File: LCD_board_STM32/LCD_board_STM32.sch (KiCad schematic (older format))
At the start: 74 parts, among them CON1 PIN-2x4, CON2 PIN-2x4, CON3 PIN-2x4, CON4 SWD-6pin, CON5 PIN-1x2, Q1 PDTC114ET, Q2 CSTCE, SW1 MicroswitchSmt6x4_V, SW2 MicroswitchSmt6x4_V, SW3 MicroswitchSmt6x4_V, U1 STM32_LQFP48, U2 TFT_1_8_ST7735, U3 NCS199A1, U4 NCS199A1, U5 AMS1117-3.3, U6 LP2980AIM5-3.0

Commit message: Working on circuit.
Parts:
- removed C10: C, 0805_M, symbol C
- added C19, C20, C21, C22: 100n, 0603_N, symbol C
- added C23, C24, C25: C, 0805_N, symbol C
- added C26: C, 0603_N, symbol C
- added Q3, Q4, Q5, Q6: FDC6331L, SOT23-6_N, symbol FDC6331L
- added R38, R39, R40, R41: R, 0603_R_N, symbol R
- C18: footprint 0805_M -> 0805_N
- C9: value C -> 100n; footprint 0805_M -> 0603_N
- gave numbers to parts that had none: 1
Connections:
- net GND: now also U1.35 (PF6/VSS), C19.2, C20.2, C21.2, C22.2, C23.2, C24.2, C25.2, C26.2, Q3.1 (R2), Q4.1 (R2), Q5.1 (R2), Q6.1 (R2), R38.1
- net PIN10: now also Q5.2 (OUT), Q5.3 (OUT)
- net PIN11: now also Q6.2 (OUT), Q6.3 (OUT)
- net PIN8: now also Q3.2 (OUT), Q3.3 (OUT)
- net PIN9: now also Q4.2 (OUT), Q4.3 (OUT)
- net VCC: now also U1.36 (PF7/VDD/VDDIO2/VDD_USB), C19.1, C20.1, C21.1, C22.1, C23.1, C24.1, C25.1, R39.2
- net VPP: now also Q3.4 (Vin), Q4.4 (Vin), Q5.4 (Vin), Q6.4 (Vin)
- net uC10: now also Q5.5 (IN)
- net uC11: now also Q6.5 (IN)
- net uC8: now also Q3.5 (IN)
- net uC9: now also Q4.5 (IN)
- net at U1.17 (PA7/VDD): now also R40.2
- net at U1.25 (PB12/VREFSD+): now also C26.1, R39.1, R41.1
- net at U1.44 (PF11/PH3/BOOT0): now also R38.2
- no-connect marks 1 -> 5
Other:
- moved on the sheet: Q2

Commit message: Working on circuit.
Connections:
- net SWO is gone; now on net SWO/SCK: CON4.6 (SWO), U1.39 (PB3)
- net PIN4: now also U3.5 (IN-); no longer U3.4 (IN+)
- net PIN5: now also U3.4 (IN+); no longer U3.5 (IN-)
- net PIN6: now also U4.5 (IN-); no longer U4.4 (IN+)
- net PIN7: now also U4.4 (IN+); no longer U4.5 (IN-)
- net SW1: now also U1.10 (PA0)
- net SW2: now also U1.38 (PA15)
- net SW3: now also U1.20 (PB2/NPOR)
- net uC0: now also U1.46 (PB9); no longer U1.10 (PA0)
- net uC10: now also U1.45 (PB8)
- net uC11: now also U1.21 (PB10/PE8)
- net uC7: now also R40.1; no longer U1.18 (PB0)
- net uC8: now also U1.18 (PB0)
- net uC9: now also U1.19 (PB1)
- net TFT_CS: now reaches U2.12 (CS)
- net TFT_CS: now also U1.2 (PC13)
- net MOSI: now reaches U2.8 (SDA)
- net MOSI: now also U1.41 (PB5)
- net SWO/SCK: now reaches U2.9 (SCK)
- net uC12: now reaches U1.22 (PB11/PE9)
- net MISO: now reaches U1.40 (PB4)
- net SD_CS: now reaches U1.3 (PC14/OSC32_IN)
- net TFT_LED: now reaches U1.4 (PC15/OSC32_OUT)
- net at D1.2 (C): now also R41.2
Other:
- moved on the sheet: D1, U2

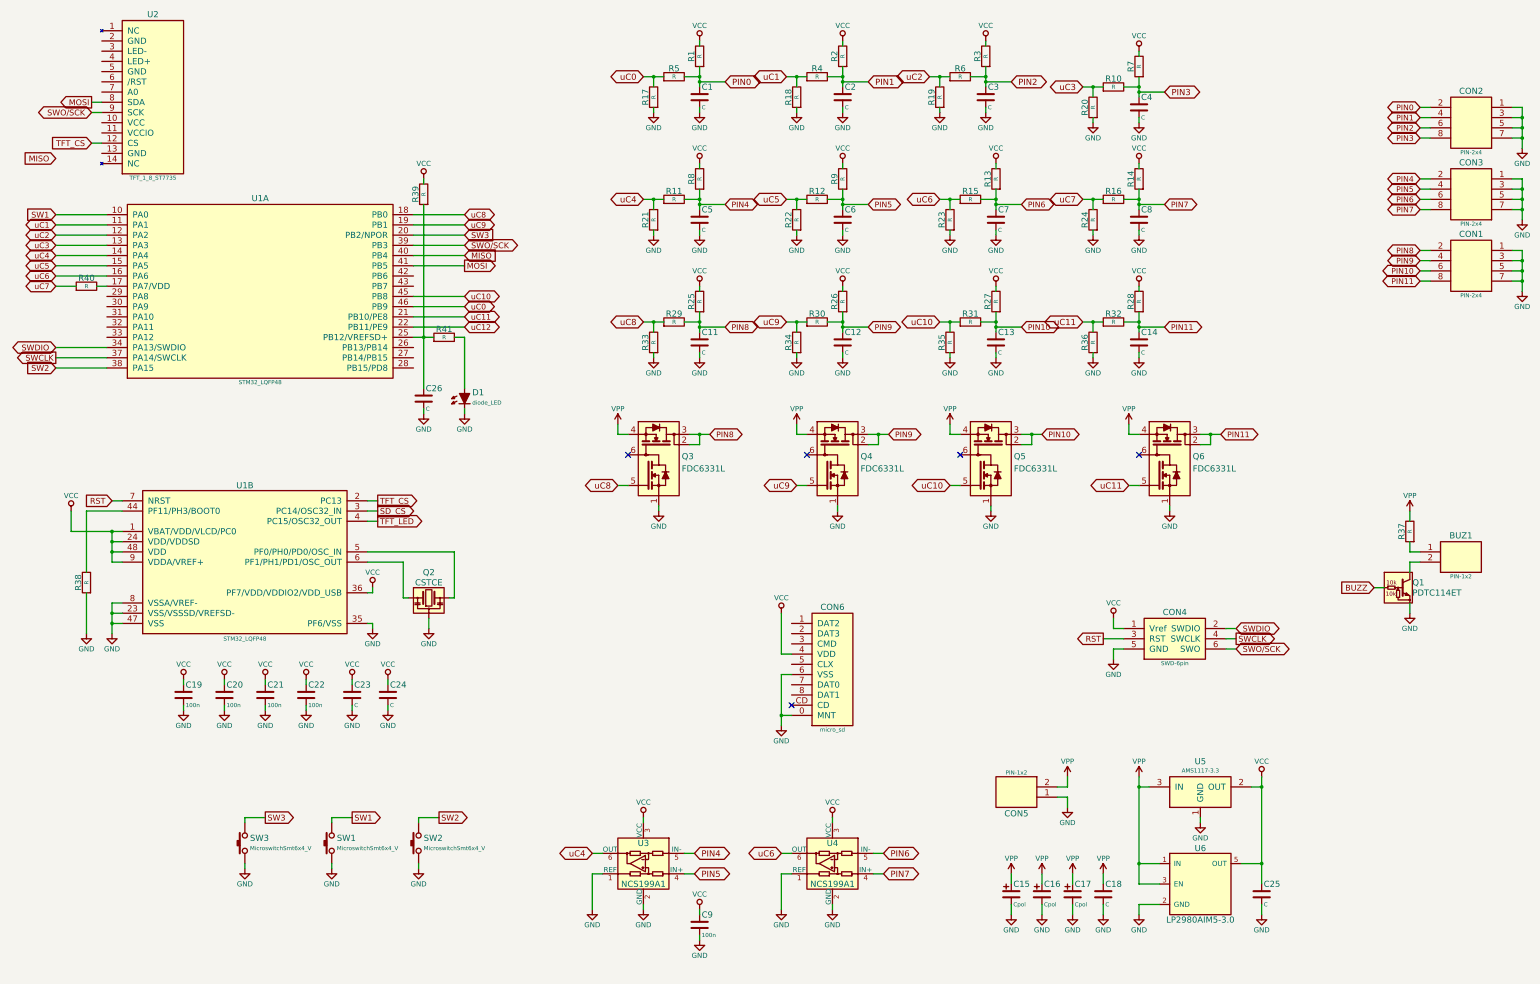
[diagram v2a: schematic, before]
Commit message: Rename nets
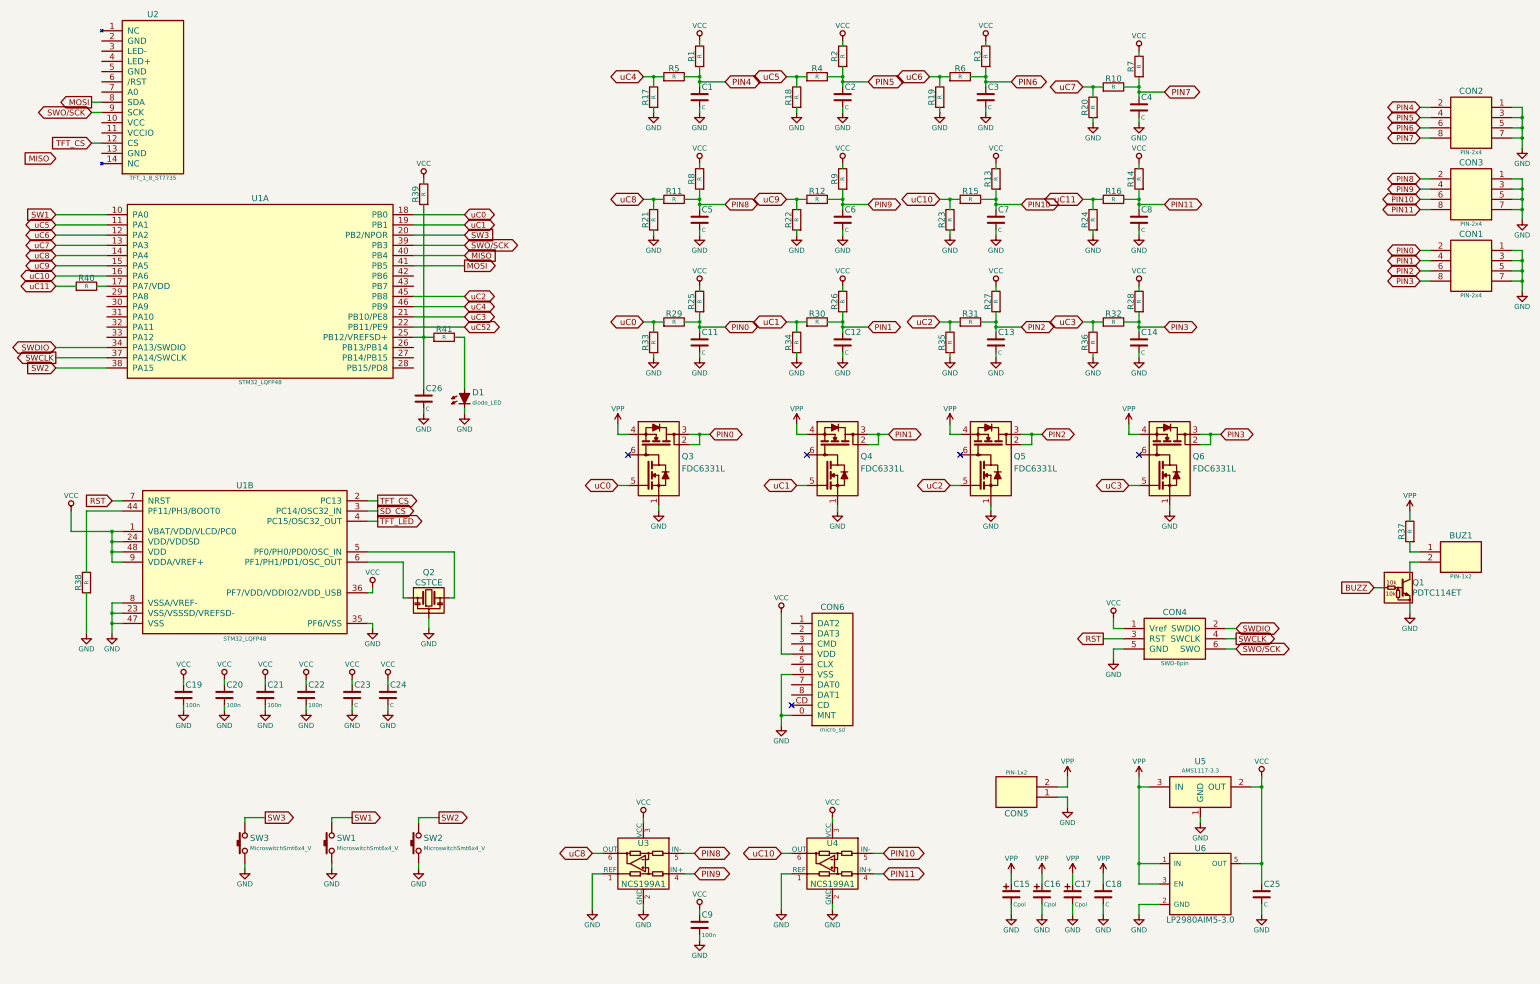
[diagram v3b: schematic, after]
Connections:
- net PIN0: now also C11.1, CON1.2, Q3.2 (OUT), Q3.3 (OUT), R25.1, R29.2; no longer C1.1, CON2.2, R1.1, R5.2
- net PIN1: now also C12.1, CON1.4, Q4.2 (OUT), Q4.3 (OUT), R26.1, R30.2; no longer C2.1, CON2.4, R2.1, R4.2
- net PIN10: now also C7.1, CON3.6, R13.1, R15.2, U4.5 (IN-); no longer C13.1, CON1.6, Q5.2 (OUT), Q5.3 (OUT), R27.1, R31.2
- net PIN11: now also C8.1, CON3.8, R14.1, R16.2, U4.4 (IN+); no longer C14.1, CON1.8, Q6.2 (OUT), Q6.3 (OUT), R28.1, R32.2
- net PIN2: now also C13.1, CON1.6, Q5.2 (OUT), Q5.3 (OUT), R27.1, R31.2; no longer C3.1, CON2.6, R3.1, R6.2
- net PIN3: now also C14.1, CON1.8, Q6.2 (OUT), Q6.3 (OUT), R28.1, R32.2; no longer C4.1, CON2.8, R10.2, R7.1
- net PIN4: now also C1.1, CON2.2, R1.1, R5.2; no longer C5.1, CON3.2, R11.2, R8.1, U3.5 (IN-)
- net PIN5: now also C2.1, CON2.4, R2.1, R4.2; no longer C6.1, CON3.4, R12.2, R9.1, U3.4 (IN+)
- net PIN6: now also C3.1, CON2.6, R3.1, R6.2; no longer C7.1, CON3.6, R13.1, R15.2, U4.5 (IN-)
- net PIN7: now also C4.1, CON2.8, R10.2, R7.1; no longer C8.1, CON3.8, R14.1, R16.2, U4.4 (IN+)
- net PIN8: now also C5.1, CON3.2, R11.2, R8.1, U3.5 (IN-); no longer C11.1, CON1.2, Q3.2 (OUT), Q3.3 (OUT), R25.1, R29.2
- net PIN9: now also C6.1, CON3.4, R12.2, R9.1, U3.4 (IN+); no longer C12.1, CON1.4, Q4.2 (OUT), Q4.3 (OUT), R26.1, R30.2
- net uC0: now also Q3.5 (IN), R29.1, R33.2, U1.18 (PB0); no longer R17.2, R5.1, U1.46 (PB9)
- net uC1: now also Q4.5 (IN), R30.1, R34.2, U1.19 (PB1); no longer R18.2, R4.1, U1.11 (PA1)
- net uC10: now also R15.1, R23.2, U1.16 (PA6), U4.6 (OUT); no longer Q5.5 (IN), R31.1, R35.2, U1.45 (PB8)
- net uC11: now also R16.1, R24.2, R40.1; no longer Q6.5 (IN), R32.1, R36.2, U1.21 (PB10/PE8)
- net uC2: now also Q5.5 (IN), R31.1, R35.2, U1.45 (PB8); no longer R19.2, R6.1, U1.12 (PA2)
- net uC3: now also Q6.5 (IN), R32.1, R36.2, U1.21 (PB10/PE8); no longer R10.1, R20.2, U1.13 (PA3)
- net uC4: now also R17.2, R5.1, U1.46 (PB9); no longer R11.1, R21.2, U1.14 (PA4), U3.6 (OUT)
- net uC5: now also R18.2, R4.1, U1.11 (PA1); no longer R12.1, R22.2, U1.15 (PA5)
- net uC6: now also R19.2, R6.1, U1.12 (PA2); no longer R15.1, R23.2, U1.16 (PA6), U4.6 (OUT)
- net uC7: now also R10.1, R20.2, U1.13 (PA3); no longer R16.1, R24.2, R40.1
- net uC8: now also R11.1, R21.2, U1.14 (PA4), U3.6 (OUT); no longer Q3.5 (IN), R29.1, R33.2, U1.18 (PB0)
- net uC9: now also R12.1, R22.2, U1.15 (PA5); no longer Q4.5 (IN), R30.1, R34.2, U1.19 (PB1)
- net uC12 renamed uC52
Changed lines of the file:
@@
 $EndComp
 Text GLabel 6900 1200 0    60   BiDi ~ 0
-uC0
+uC4
 Text GLabel 7700 1250 2    60   BiDi ~ 0
-PIN0
+PIN4
 Text GLabel 14500 2300 0    55   BiDi ~ 0
+PIN9
+Text GLabel 14500 2200 0    55   BiDi ~ 0
+PIN8
+Text GLabel 14500 2500 0    55   BiDi ~ 0
+PIN11
+Text GLabel 14500 2400 0    55   BiDi ~ 0
+PIN10
+Text GLabel 14500 1600 0    55   BiDi ~ 0
 PIN5
-Text GLabel 14500 2200 0    55   BiDi ~ 0
+Text GLabel 14500 1500 0    55   BiDi ~ 0
 PIN4
-Text GLabel 14500 2500 0    55   BiDi ~ 0
+Text GLabel 14500 1800 0    55   BiDi ~ 0
 PIN7
-Text GLabel 14500 2400 0    55   BiDi ~ 0
+Text GLabel 14500 1700 0    55   BiDi ~ 0
 PIN6
-Text GLabel 14500 1600 0    55   BiDi ~ 0
-PIN1
-Text GLabel 14500 1500 0    55   BiDi ~ 0
-PIN0
-Text GLabel 14500 1800 0    55   BiDi ~ 0
-PIN3
-Text GLabel 14500 1700 0    55   BiDi ~ 0
-PIN2
 $Comp
 L GND #PWR03
@@
 $EndComp
 Text GLabel 5150 3450 2    55   BiDi ~ 0
+uC4
+Text GLabel 1150 2650 0    55   BiDi ~ 0
+uC5
+Text GLabel 1150 2750 0    55   BiDi ~ 0
+uC6
+Text GLabel 1150 2850 0    55   BiDi ~ 0
+uC7
+Text GLabel 1150 2950 0    55   BiDi ~ 0
+uC8
+Text GLabel 1150 3050 0    55   BiDi ~ 0
+uC9
+Text GLabel 5150 2550 2    55   BiDi ~ 0
 uC0
-Text GLabel 1150 2650 0    55   BiDi ~ 0
-uC1
-Text GLabel 1150 2750 0    55   BiDi ~ 0
-uC2
-Text GLabel 1150 2850 0    55   BiDi ~ 0
-uC3
-Text GLabel 1150 2950 0    55   BiDi ~ 0
-uC4
-Text GLabel 1150 3050 0    55   BiDi ~ 0
-uC5
-Text GLabel 5150 2550 2    55   BiDi ~ 0
-uC8
 Text GLabel 1150 3150 0    55   BiDi ~ 0
-uC6
+uC10
 $Comp
 L R R4
@@
 $EndComp
 Text GLabel 8300 1200 0    60   BiDi ~ 0
-uC1
+uC5
 Text GLabel 9100 1250 2    60   BiDi ~ 0
-PIN1
+PIN5
 $Comp
 L R R6
@@
 $EndComp
 Text GLabel 9700 1200 0    60   BiDi ~ 0
-uC2
+uC6
 Text GLabel 10500 1250 2    60   BiDi ~ 0
-PIN2
+PIN6
 $Comp
 L R R10
@@
 $EndComp
 Text GLabel 11200 1300 0    60   BiDi ~ 0
-uC3
+uC7
 Text GLabel 12000 1350 2    60   BiDi ~ 0
-PIN3
+PIN7
 $Comp
 L R R11
@@
 $EndComp
 Text GLabel 6900 2400 0    60   BiDi ~ 0
-uC4
+uC8
 Text GLabel 7400 8800 2    60   BiDi ~ 0
-PIN4
+PIN8
 $Comp
 L R R12
@@
 $EndComp
 Text GLabel 8300 2400 0    60   BiDi ~ 0
-uC5
+uC9
 Text GLabel 7400 9000 2    60   BiDi ~ 0
-PIN5
+PIN9
 $Comp
 L R R15
@@
 $EndComp
 Text GLabel 9800 2400 0    60   BiDi ~ 0
-uC6
+uC10
 Text GLabel 9250 8800 2    60   BiDi ~ 0
-PIN6
+PIN10
 $Comp
 L R R16
@@
 $EndComp
 Text GLabel 11200 2400 0    60   BiDi ~ 0
-uC7
+uC11
 Text GLabel 9250 9000 2    60   BiDi ~ 0
-PIN7
+PIN11
 $Comp
 L R R17
@@
 $EndComp
 Text GLabel 8250 8800 0    60   BiDi ~ 0
-uC6
+uC10
 Text GLabel 6400 8800 0    60   BiDi ~ 0
-uC4
+uC8
 $Comp
 L GND #PWR029
@@
 RST
 Text GLabel 9100 2450 2    55   BiDi ~ 0
-PIN5
+PIN9
 Text GLabel 7700 2450 2    55   BiDi ~ 0
-PIN4
+PIN8
 Text GLabel 12000 2450 2    55   BiDi ~ 0
-PIN7
+PIN11
 Text GLabel 10600 2450 2    55   BiDi ~ 0
-PIN6
+PIN10
 $Comp
 L R R29
@@
 $EndComp
 Text GLabel 6900 3600 0    60   BiDi ~ 0
-uC8
+uC0
 $Comp
 L R R30
@@
 $EndComp
 Text GLabel 8300 3600 0    60   BiDi ~ 0
-uC9
+uC1
 $Comp
 L R R31
@@
 $EndComp
 Text GLabel 9800 3600 0    60   BiDi ~ 0
-uC10
+uC2
 $Comp
 L R R32
@@
 $EndComp
 Text GLabel 11200 3600 0    60   BiDi ~ 0
-uC11
+uC3
 $Comp
 L R R35
@@
 $EndComp
 Text GLabel 9100 3650 2    55   BiDi ~ 0
-PIN9
+PIN1
 Text GLabel 7700 3650 2    55   BiDi ~ 0
-PIN8
+PIN0
 Text GLabel 12000 3650 2    55   BiDi ~ 0
-PIN11
+PIN3
 Text GLabel 10600 3650 2    55   BiDi ~ 0
-PIN10
+PIN2
 Text GLabel 14500 2900 0    55   BiDi ~ 0
-PIN8
+PIN0
 Text GLabel 14500 3000 0    55   BiDi ~ 0
-PIN9
+PIN1
 Text GLabel 14500 3100 0    55   BiDi ~ 0
-PIN10
+PIN2
 Text GLabel 14500 3200 0    55   BiDi ~ 0
-PIN11
+PIN3
 $Comp
 L GND #PWR050
@@
 $EndComp
 Text GLabel 6650 5200 0    60   BiDi ~ 0
-uC8
+uC0
 Text GLabel 7550 4700 2    55   BiDi ~ 0
-PIN8
+PIN0
 NoConn ~ 6750 4900
 Wire Wire Line
@@
 	11650 4700 11650 4600
 Text GLabel 8400 5200 0    60   BiDi ~ 0
-uC9
+uC1
 Text GLabel 9300 4700 2    55   BiDi ~ 0
-PIN9
+PIN1
 Text GLabel 9900 5200 0    60   BiDi ~ 0
-uC10
+uC2
 Text GLabel 10800 4700 2    55   BiDi ~ 0
-PIN10
+PIN2
 Text GLabel 11650 5200 0    60   BiDi ~ 0
-uC11
+uC3
 Text GLabel 12550 4700 2    55   BiDi ~ 0
-PIN11
+PIN3
 $Comp
 L C C19
@@
 	1150 3250 1350 3250
 Text GLabel 1150 3250 0    55   BiDi ~ 0
-uC7
+uC11
 Text GLabel 5150 2650 2    55   BiDi ~ 0
-uC9
+uC1
 Wire Wire Line
 	5150 2650 4650 2650
 Text GLabel 5150 3550 2    55   BiDi ~ 0
-uC11
+uC3
 Text GLabel 5150 3650 2    55   BiDi ~ 0
-uC12
+uC52
 Wire Wire Line
 	4650 3550 5150 3550
@@
 	5150 3750 5150 4250
 Text GLabel 5150 3350 2    55   BiDi ~ 0
-uC10
+uC2
 Wire Wire Line
 	1650 4050 1150 4050
